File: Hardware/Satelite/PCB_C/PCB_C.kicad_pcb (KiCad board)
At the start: 2 copper layers, 54 x 54 mm, 49 parts, among them IC1 MCP1501T-33E_CHY, IC2 IS25LP080D-JULE-TR, IC3 BQ24392RSER, IC4 MS563702BA03-50, IC5 BMX055, J1 Conn_01x06, J2 BOOT, J3 Conector_PCB_B-C, J4 Conector_Expansion_CanSat, J5 USB_B_Micro, M1 Spacer, M2 Spacer, M3 Spacer, U1 NTB0104BQ,115, U2 TCA9802DGKR, U3 STM32F303RETx, U4 NTB0104BQ,115, U6 Si7006-A20-IM1, Y1 LFXTAL016178, Y2 Crystal

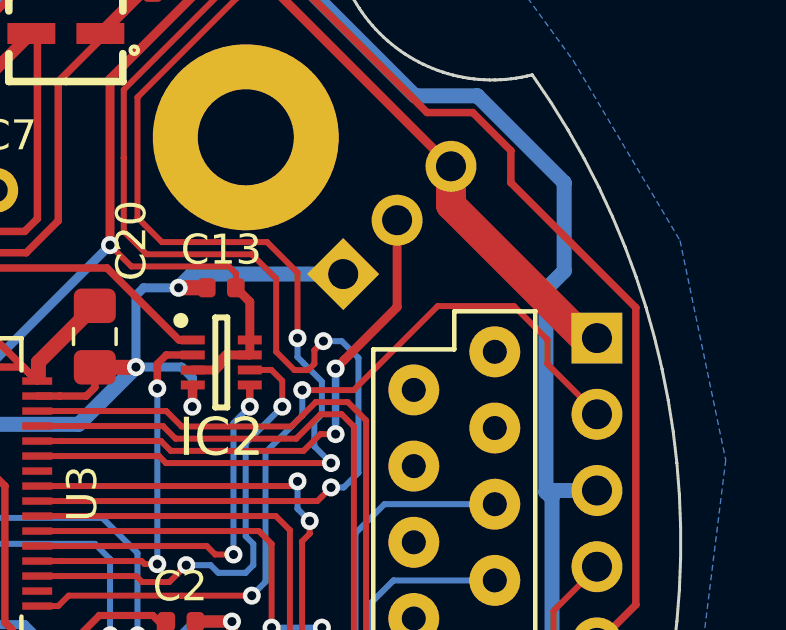
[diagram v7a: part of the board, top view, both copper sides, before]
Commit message: Agregado pull-down para pin BOOT0
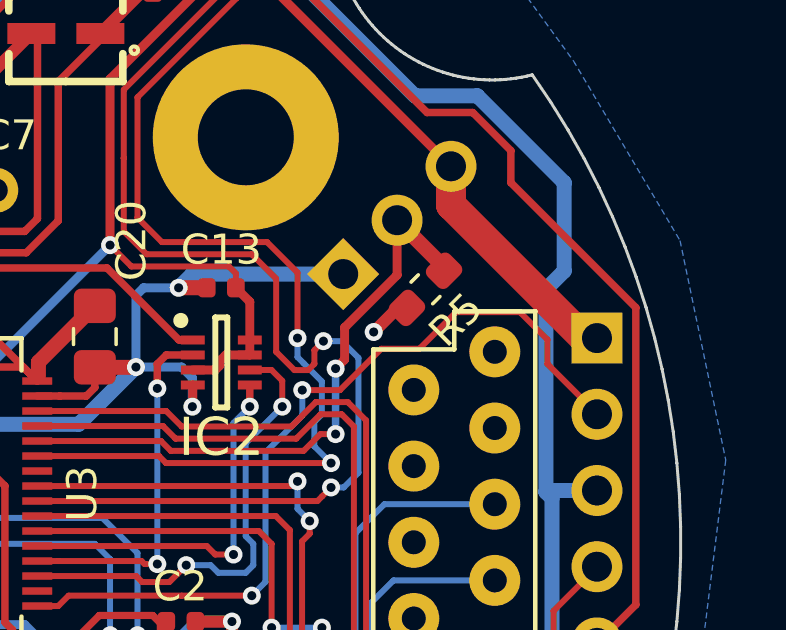
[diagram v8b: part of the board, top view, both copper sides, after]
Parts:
- added R5: 10k, Resistor_SMD:R_0603_1608Metric_Pad1.05x0.95mm_HandSolder, F.Cu at (18.5, -8.43)
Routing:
- net Net-(J2-Pad2): track 18.3 -> 20.6 mm
- net GND: track 359.1 -> 360.5 mm, vias 34 -> 35
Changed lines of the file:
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@@
     (thickness 1.6)
     (drawings 0)
-    (tracks 1610)
+    (tracks 1618)
     (zones 0)
-    (modules 49)
+    (modules 50)
     (nets 105)
   )
@@
     (add_net VBUS)
   )
+  (module Resistor_SMD:R_0603_1608Metric_Pad1.05x0.95mm_HandSolder (layer F.Cu)
+    (at 18.4912 -8.4328 225)
+    (descr "Resistor SMD 0603 (1608 Metric), square (rectangular) end terminal, IPC_7351 nominal with elongated pad for handsoldering. (Body size source: http://www.tortai-tech.com/upload/download/2011102023233369053.pdf), generated with kicad-footprint-generator")
+    (tags "resistor handsolder")
+    (attr smd)
+    (fp_text reference R5 (at 0 -1.43 225) (layer F.SilkS)
+      (effects (font (size 1 1) (thickness 0.15)))
+    )
+    (fp_text value 10k (at 0 1.43 225) (layer F.Fab)
+      (effects (font (size 1 1) (thickness 0.15)))
+    )
+    (fp_line (start -0.8 0.4) (end -0.8 -0.4) (layer F.Fab) (width 0.1))
+    (fp_line (start -0.8 -0.4) (end 0.8 -0.4) (layer F.Fab) (width 0.1))
+    (fp_line (start 0.8 -0.4) (end 0.8 0.4) (layer F.Fab) (width 0.1))
+    (fp_line (start 0.8 0.4) (end -0.8 0.4) (layer F.Fab) (width 0.1))
+    (fp_line (start -0.171267 -0.51) (end 0.171267 -0.51) (layer F.SilkS) (width 0.12))
+    (fp_line (start -0.171267 0.51) (end 0.171267 0.51) (layer F.SilkS) (width 0.12))
+    (fp_line (start -1.65 0.73) (end -1.65 -0.73) (layer F.CrtYd) (width 0.05))
+    (fp_line (start -1.65 -0.73) (end 1.65 -0.73) (layer F.CrtYd) (width 0.05))
+    (fp_line (start 1.65 -0.73) (end 1.65 0.73) (layer F.CrtYd) (width 0.05))
+    (fp_line (start 1.65 0.73) (end -1.65 0.73) (layer F.CrtYd) (width 0.05))
+    (fp_text user %R (at 0 0 225) (layer F.Fab)
+      (effects (font (size 0.4 0.4) (thickness 0.06)))
+    )
+    (pad 1 smd roundrect (at -0.875 0 225) (size 1.05 0.95) (layers F.Cu F.Paste F.Mask) (roundrect_rratio 0.25)
+      (net 39 "Net-(J2-Pad2)"))
+    (pad 2 smd roundrect (at 0.875 0 225) (size 1.05 0.95) (layers F.Cu F.Paste F.Mask) (roundrect_rratio 0.25)
+      (net 1 GND))
+    (model ${KISYS3DMOD}/Resistor_SMD.3dshapes/R_0603_1608Metric.wrl
+      (at (xyz 0 0 0))
+      (scale (xyz 1 1 1))
+      (rotate (xyz 0 0 0))
+    )
+  )
   (module AXTEC:Empty_Footprint (layer F.Cu)
     (at 24.0084 -23.5752)
@@
   (segment (start 22.7076 -1.4732) (end 22.5044 -1.6764) (width 0.5) (layer B.Cu) (net 1))
   (segment (start 14.635599 16.999199) (end 16.274801 16.999199) (width 0.5) (layer B.Cu) (net 1))
+  (via (at 16.764 -7.0104) (size 0.6) (drill 0.3) (layers F.Cu B.Cu) (net 1))
+  (segment (start 17.872482 -7.814082) (end 17.567682 -7.814082) (width 0.4) (layer F.Cu) (net 1))
+  (segment (start 17.567682 -7.814082) (end 16.764 -7.0104) (width 0.4) (layer F.Cu) (net 1))
   (via (at 3.2004 -20.9804) (size 0.6) (drill 0.3) (layers F.Cu B.Cu) (net 2))
   (via (at 3.2004 -20.3708) (size 0.6) (drill 0.3) (layers F.Cu B.Cu) (net 2))
@@
   (segment (start -2.7432 14.089136) (end -5.842 10.990336) (width 0.2) (layer F.Cu) (net 25))
   (segment (start -5.842 10.990336) (end -5.842 5.7912) (width 0.2) (layer F.Cu) (net 25))
-  (segment (start 18.8976 -7.874) (end 16.09721 -5.07361) (width 0.2) (layer F.Cu) (net 36))
-  (segment (start 21.4376 -7.874) (end 18.8976 -7.874) (width 0.2) (layer F.Cu) (net 36))
-  (segment (start 22.5552 -6.7564) (end 21.4376 -7.874) (width 0.2) (layer F.Cu) (net 36))
-  (segment (start 24.2316 -4.2672) (end 22.5552 -5.9436) (width 0.2) (layer F.Cu) (net 36))
-  (segment (start 22.5552 -5.9436) (end 22.5552 -6.7564) (width 0.2) (layer F.Cu) (net 36))
   (via (at 12.7 1.778) (size 0.6) (drill 0.3) (layers F.Cu B.Cu) (net 36))
   (segment (start 6.2476 2.1244) (end 6.594 1.778) (width 0.2) (layer F.Cu) (net 36))
@@
   (segment (start 13.1572 -2.9972) (end 13.1572 1.3208) (width 0.2) (layer B.Cu) (net 36))
   (segment (start 13.1572 1.3208) (end 12.7 1.778) (width 0.2) (layer B.Cu) (net 36))
-  (segment (start 16.09721 -5.07361) (end 14.38279 -5.07361) (width 0.2) (layer F.Cu) (net 36))
+  (segment (start 22.5552 -5.9436) (end 24.2316 -4.2672) (width 0.2) (layer F.Cu) (net 36))
+  (segment (start 22.5552 -6.7564) (end 22.5552 -5.9436) (width 0.2) (layer F.Cu) (net 36))
+  (segment (start 15.64001 -5.07361) (end 17.018 -6.4516) (width 0.2) (layer F.Cu) (net 36))
+  (segment (start 17.018 -6.4516) (end 18.288 -6.4516) (width 0.2) (layer F.Cu) (net 36))
+  (segment (start 14.38279 -5.07361) (end 15.64001 -5.07361) (width 0.2) (layer F.Cu) (net 36))
+  (segment (start 18.288 -6.4516) (end 19.5072 -7.6708) (width 0.2) (layer F.Cu) (net 36))
+  (segment (start 19.5072 -7.6708) (end 21.6408 -7.6708) (width 0.2) (layer F.Cu) (net 36))
+  (segment (start 21.6408 -7.6708) (end 22.5552 -6.7564) (width 0.2) (layer F.Cu) (net 36))
   (via (at 14.3256 10.6172) (size 0.6) (drill 0.3) (layers F.Cu B.Cu) (net 37))
   (segment (start 7.9825 10.6172) (end 13.901336 10.6172) (width 0.2) (layer F.Cu) (net 37))
@@
   (via (at 15.494 -5.791206) (size 0.6) (drill 0.3) (layers F.Cu B.Cu) (net 39))
   (segment (start 15.494 -3.6068) (end 15.494 -5.791206) (width 0.25) (layer B.Cu) (net 39))
-  (segment (start 17.544051 -10.736851) (end 17.544051 -7.841257) (width 0.3) (layer F.Cu) (net 39))
-  (segment (start 17.544051 -7.841257) (end 15.793999 -6.091205) (width 0.3) (layer F.Cu) (net 39))
   (segment (start 15.793999 -6.091205) (end 15.494 -5.791206) (width 0.3) (layer F.Cu) (net 39))
+  (segment (start 15.793999 -7.157999) (end 15.793999 -6.091205) (width 0.3) (layer F.Cu) (net 39))
+  (segment (start 17.544051 -10.736851) (end 17.544051 -8.908051) (width 0.3) (layer F.Cu) (net 39))
+  (segment (start 17.544051 -8.908051) (end 15.793999 -7.157999) (width 0.3) (layer F.Cu) (net 39))
+  (segment (start 19.109918 -9.170984) (end 17.544051 -10.736851) (width 0.5) (layer F.Cu) (net 39))
+  (segment (start 19.109918 -9.051518) (end 19.109918 -9.170984) (width 0.5) (layer F.Cu) (net 39))
   (via (at -3.302 -22.1) (size 0.6) (drill 0.3) (layers F.Cu B.Cu) (net 40))
   (segment (start -1.75 -20.75) (end -3.302 -20.75) (width 0.3) (layer F.Cu) (net 40))
